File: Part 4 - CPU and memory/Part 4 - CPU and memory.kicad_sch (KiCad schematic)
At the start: 50 parts, among them J1 EDGE, U1 74AHC00, U10 SST39SF010, U11 AS6C4008, U2 74AHC32, U3 74AHC32, U4 74AHC32, U5 74HC563, U6 74AHC174, U7 74AHC138, U8 Z80C0010, U9 74HC563

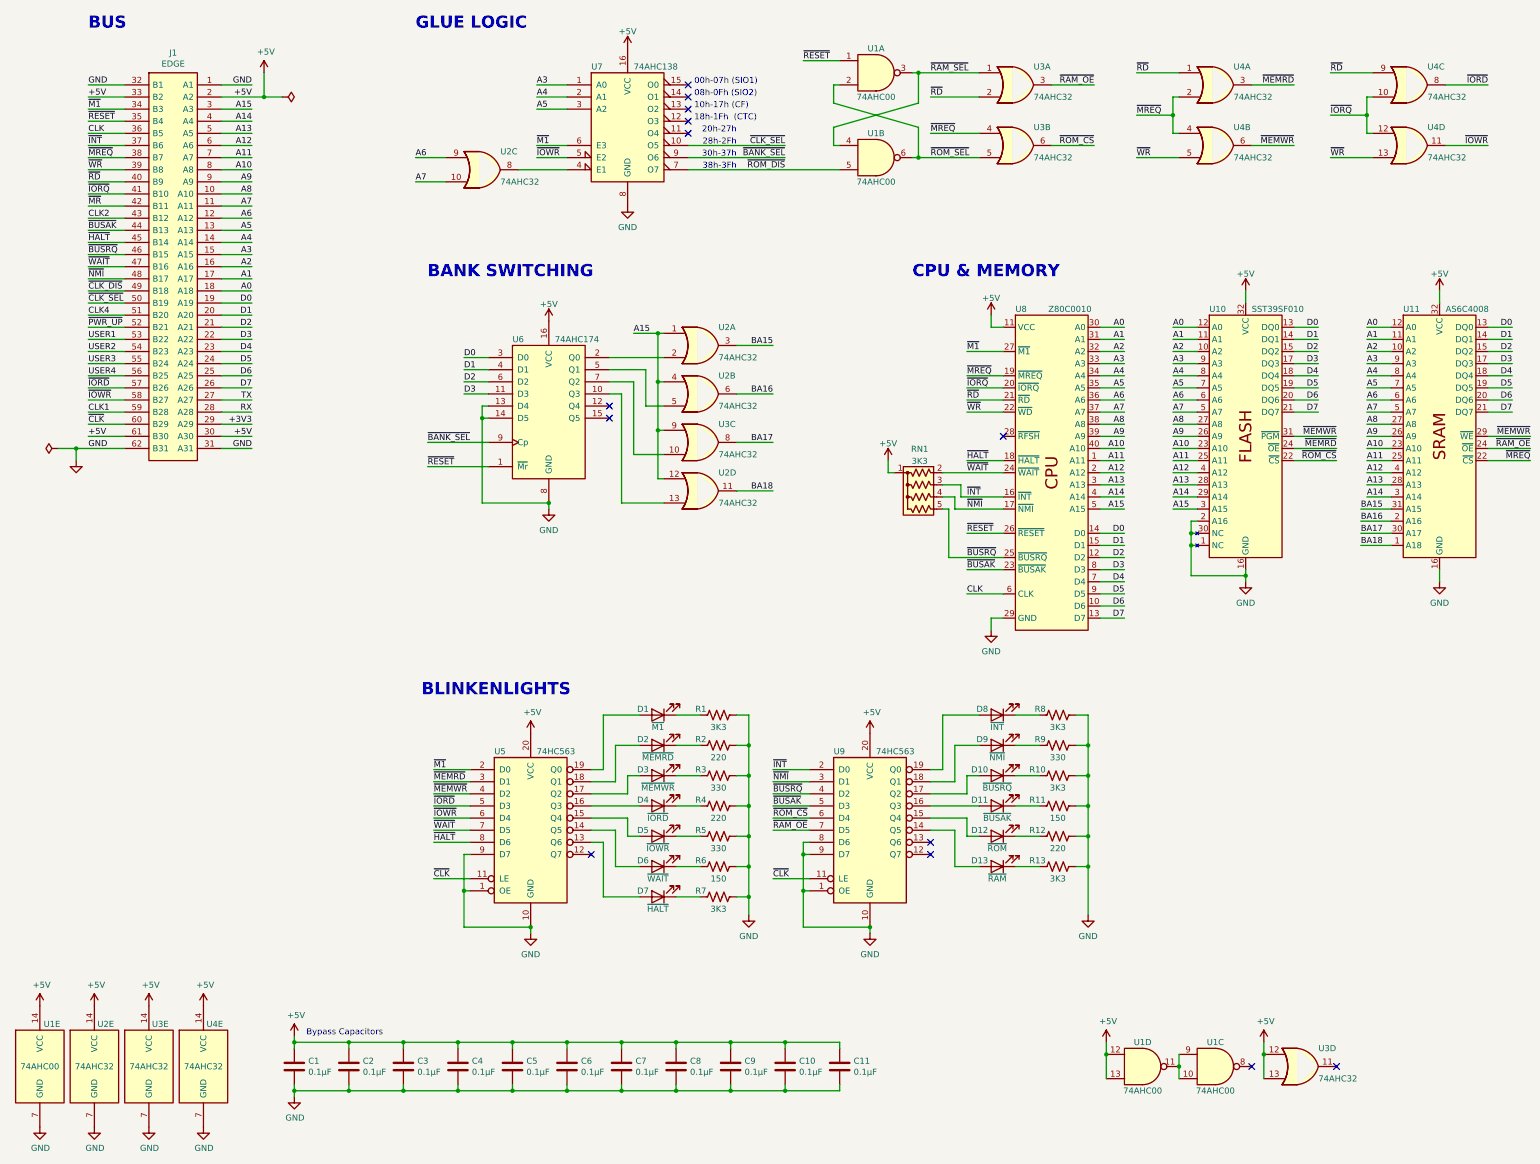
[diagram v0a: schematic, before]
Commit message: Changed the clock for even cleaner clock switching
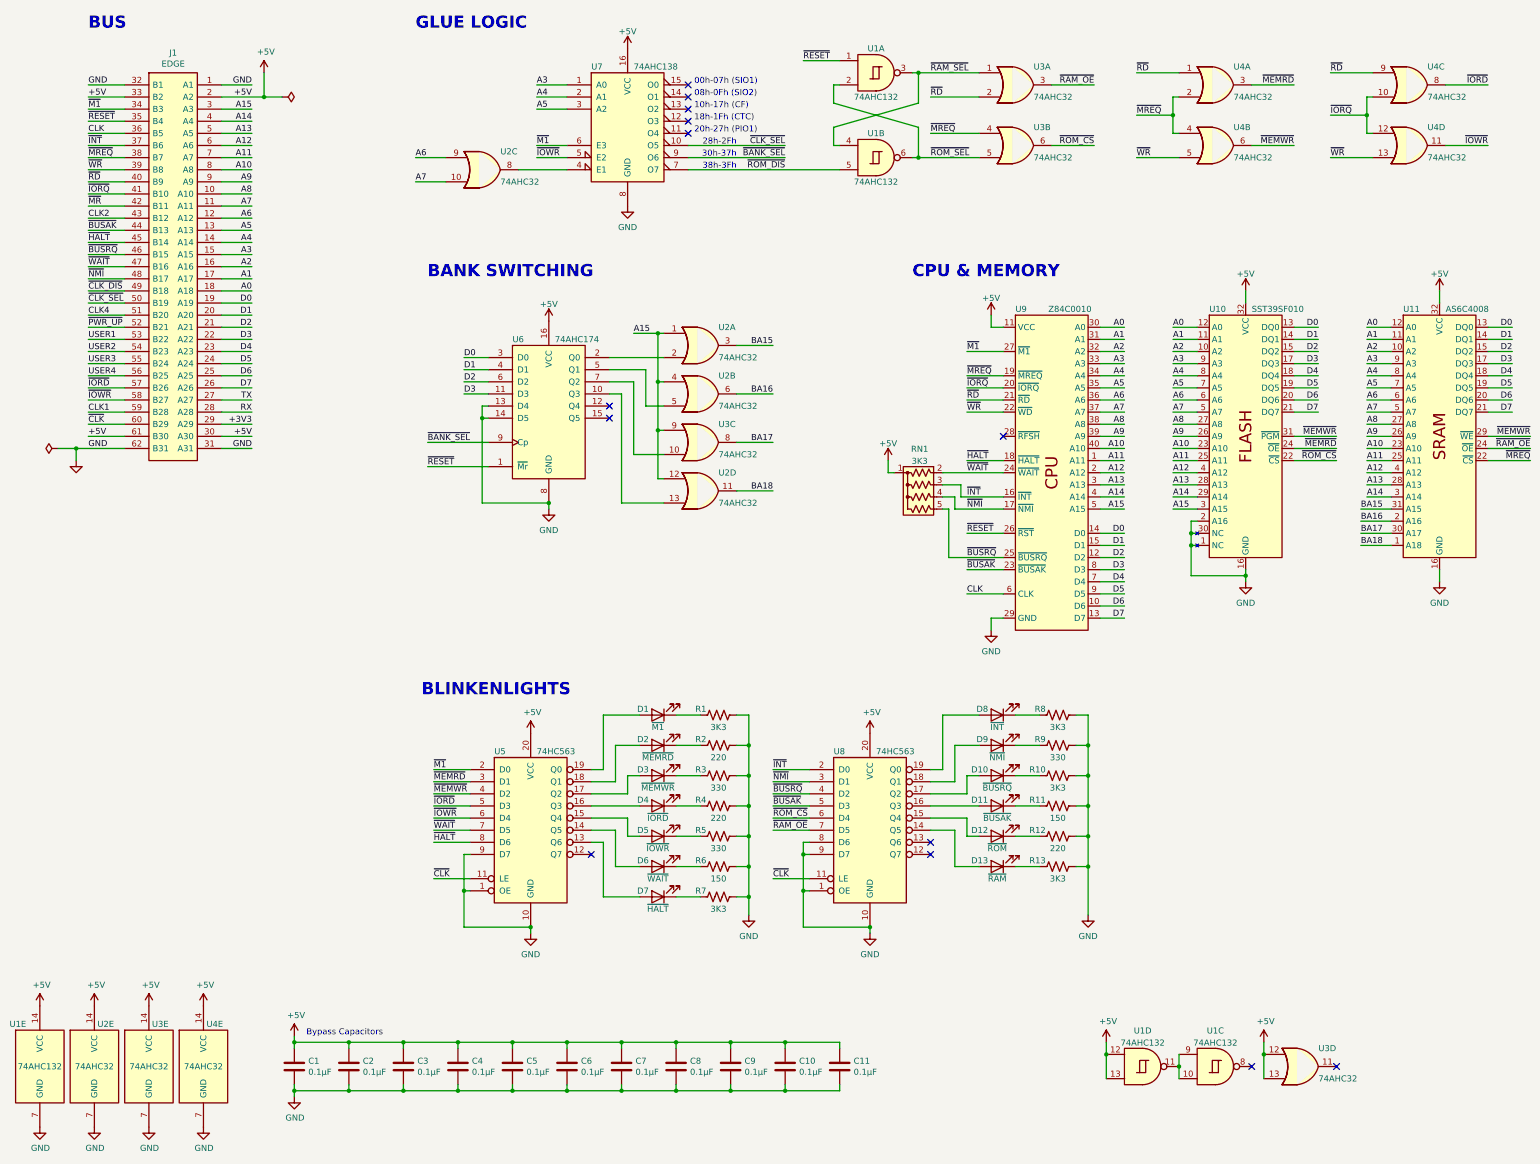
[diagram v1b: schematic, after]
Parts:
- removed U1: 74AHC00, Package_DIP:DIP-14_W7.62mm_Socket, symbol 74xx:74HC00
- added U1: 74AHC132, Package_DIP:DIP-14_W7.62mm_Socket, symbol 74xx:74LS132
- U9: renamed from U8; value Z80C0010 -> Z84C0010; symbol 0_Z80_Library:Z80C00xx -> 0_Z80_Library:Z84C00xx CPU
- renumbered U9 to U8
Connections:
- net +5V: now also U1.12, U1.13, U1.14 (VCC)
- net GND: now also U1.7 (GND)
- net ~{RAM_SEL}: now also U1.3, U1.4
- net ~{RESET}: now also U1.1
- net ~{ROM_DIS}: now also U1.5
- net ~{ROM_SEL}: now also U1.2, U1.6
- new net: U1.10, U1.11, U1.9
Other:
- note added: "20h-27h (PIO1)"
- note removed: "20h-27h"

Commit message: Clock 3 and Keyboard
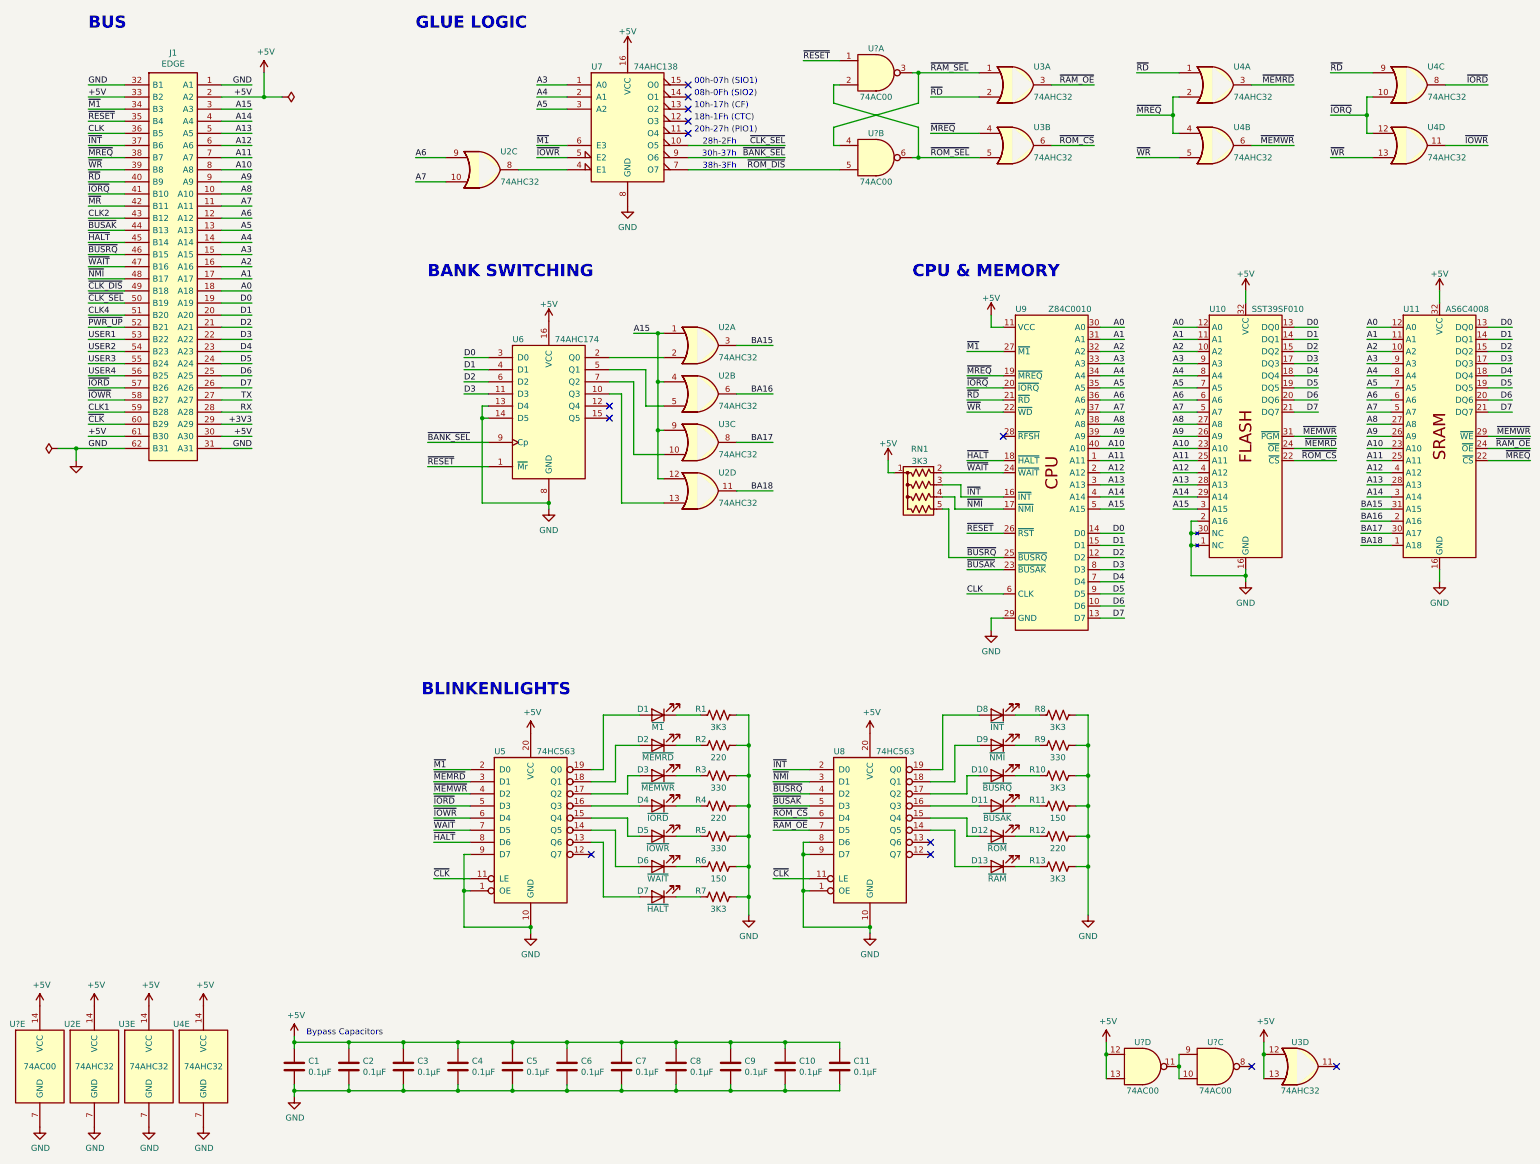
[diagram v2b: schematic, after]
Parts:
- removed U1: 74AHC132, Package_DIP:DIP-14_W7.62mm_Socket, symbol 74xx:74LS132
- added U? (x5): 74AC00, Package_DIP:DIP-14_W7.62mm_Socket, symbol 74xx:74HC00
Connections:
- net +5V: now also U?.12, U?.13, U?.14 (VCC)
- net GND: now also U?.7 (GND)
- net ~{RAM_SEL}: now also U?.3, U?.4
- net ~{RESET}: now also U?.1
- net ~{ROM_DIS}: now also U?.5
- net ~{ROM_SEL}: now also U?.2, U?.6
- new net: U?.10, U?.11, U?.9

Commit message: Added Keyboard, and minor fixes
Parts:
- removed C9: 0.1µF, Capacitor_THT:C_Disc_D3.0mm_W1.6mm_P2.50mm, symbol Device:C
- removed unit 4 of U3
- removed unit 5 of U3
- removed unit 2 of U4
- removed unit 4 of U4
- removed unit 1 of U4
- removed unit 3 of U4
- added unit 3 of U2
- D3: renamed from D2; value ~{MEMRD} -> ~{MEMRQ}
- D5: renamed from D3; value ~{MEMWR} -> ~{IORQ}
- D7: renamed from D4; value ~{IORD} -> ~{RD}
- D9: renamed from D5; value ~{IOWR} -> ~{WR}
- U2, U7: renamed from U3; value 74AHC32 -> 74AC32
- U2: value 74AHC32 -> 74AC32
- U3: renamed from U7; value 74AHC138 -> 74AC138
- U7: renamed from U4; value 74AHC32 -> 74AC32
- U7: renamed from U2; value 74AHC32 -> 74AC32
- U8: renamed from U6; value 74AHC174 -> 74AC174
- gave numbers to parts that had none: 1
- renumbered C11 to C10, C10 to C9, D12 to D10, D6 to D11, D13 to D12, D7 to D13, D8 to D2, D9 to D4, D10 to D6, D11 to D8, R12 to R10, R6 to R11, R13 to R12, R7 to R13, R8 to R2, R2 to R3, R9 to R4, R3 to R5, R10 to R6, R4 to R7, R11 to R8, R5 to R9, U8 to U10, U9 to U4, U10 to U5, U11 to U6, U5 to U9
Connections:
- net A6: now also U2.12; no longer U2.9
- net A7: now also U2.13; no longer U2.10
- net ~{BUSRQ}: now also RN1.3 (R2); no longer RN1.5 (R4)
- net ~{INT}: now also RN1.4 (R3); no longer RN1.3 (R2)
- net ~{IORQ}: now also U9.4 (D2), U2.9
- net ~{IOWR}: now also U2.8; no longer J1.58 (B27), U9.6 (D4)
- net ~{MREQ}: now also U9.3 (D1)
- net ~{NMI}: now also RN1.5 (R4); no longer RN1.4 (R3)
- net ~{RD}: now also U5.24 (~{OE}), U9.5 (D3)
- net ~{WR}: now also U5.31 (~{PGM}), U6.29 (~{WE}), U9.6 (D4), U2.10
- net at U3.4 (E1): now also U2.11; no longer U2.8
- net ~{IORD} renamed USER5
- net USER5: no longer U9.5 (D3)
- removed net ~{MEMRD}: U5.24 (~{OE}), U9.3 (D1)
- removed net ~{MEMWR}: U5.31 (~{PGM}), U6.29 (~{WE}), U9.4 (D2)
- new net USER6: J1.58 (B27)
- no-connect marks 13 -> 12
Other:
- moved on the sheet: C10, C9, RN1, U1C, U1D, U2D, U7E

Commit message: Updated key library and keyboard
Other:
- company: Frederic Segard, aka: The Micro Hobbyist -> Frederic Segard
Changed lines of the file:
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@@
     (date "2022-10-27")
     (rev "1.1")
-    (company "Frederic Segard, aka: The Micro Hobbyist")
-    (comment 4 "Done with the inspiration of Grant Searl and John Winans")
+    (company "Frederic Segard")
+    (comment 1 "youtube.com/@microhobbyist.com")
+    (comment 4 "Designed with the inspiration of Grant Searl and John Winans")
   )
   (junction (at 241.3 177.8) (diameter 0) (color 0 0 0 0)
